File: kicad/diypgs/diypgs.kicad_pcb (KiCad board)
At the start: 2 copper layers, 150 x 78 mm, 15 parts, among them SW1 SW_Push_Dual, SW2 SW_Push_Dual, SW3 SW_Push_Dual, SW4 SW_Push_Dual, SW5 SW_Push_Dual, SW6 SW_Push_Dual, U1 Nokia 5110 LCD

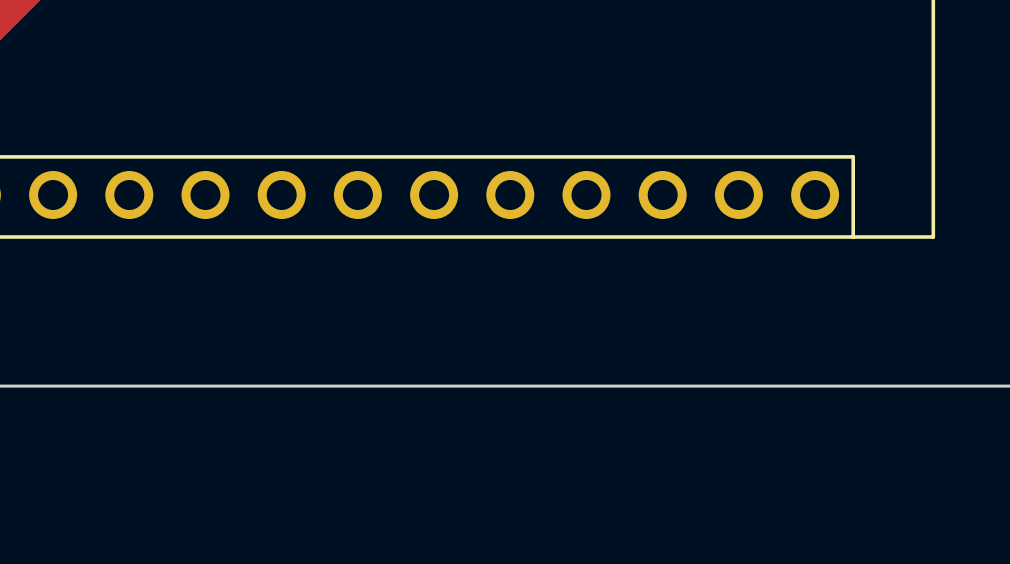
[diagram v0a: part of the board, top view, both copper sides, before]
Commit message: Add JST connector
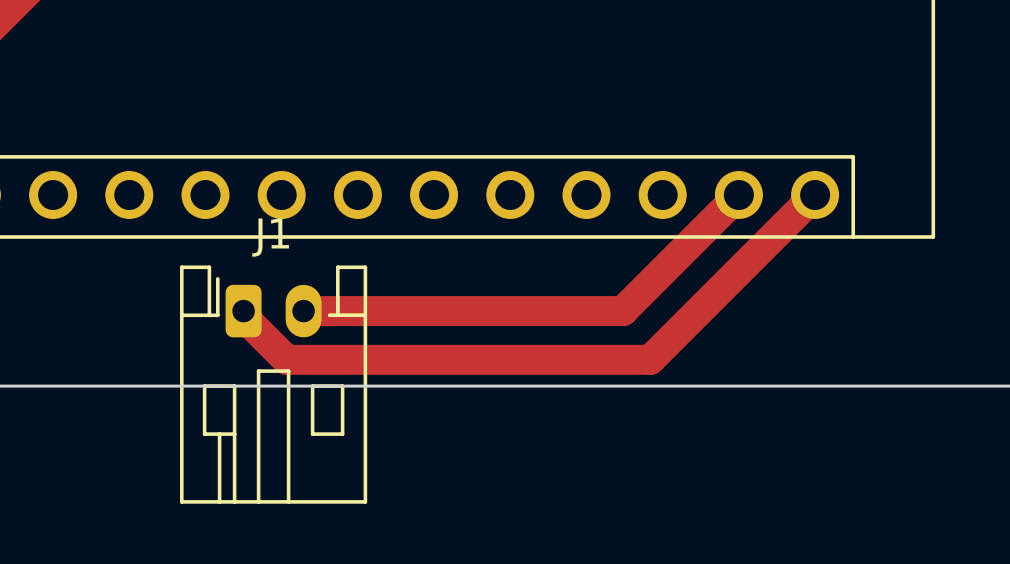
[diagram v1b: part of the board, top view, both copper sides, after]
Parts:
- added J1: Conn_01x02, Connector_JST:JST_PH_S2B-PH-K_1x02_P2.00mm_Horizontal, F.Cu at (124.0, 113.5)
- U1: value Nokia 5110 LCD -> Sparkfun - Graphic LCD 84x48 - Nokia 5110
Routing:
- net VCC: track 0.00 -> 22.1 mm
- net GND: track 303.3 -> 319.4 mm

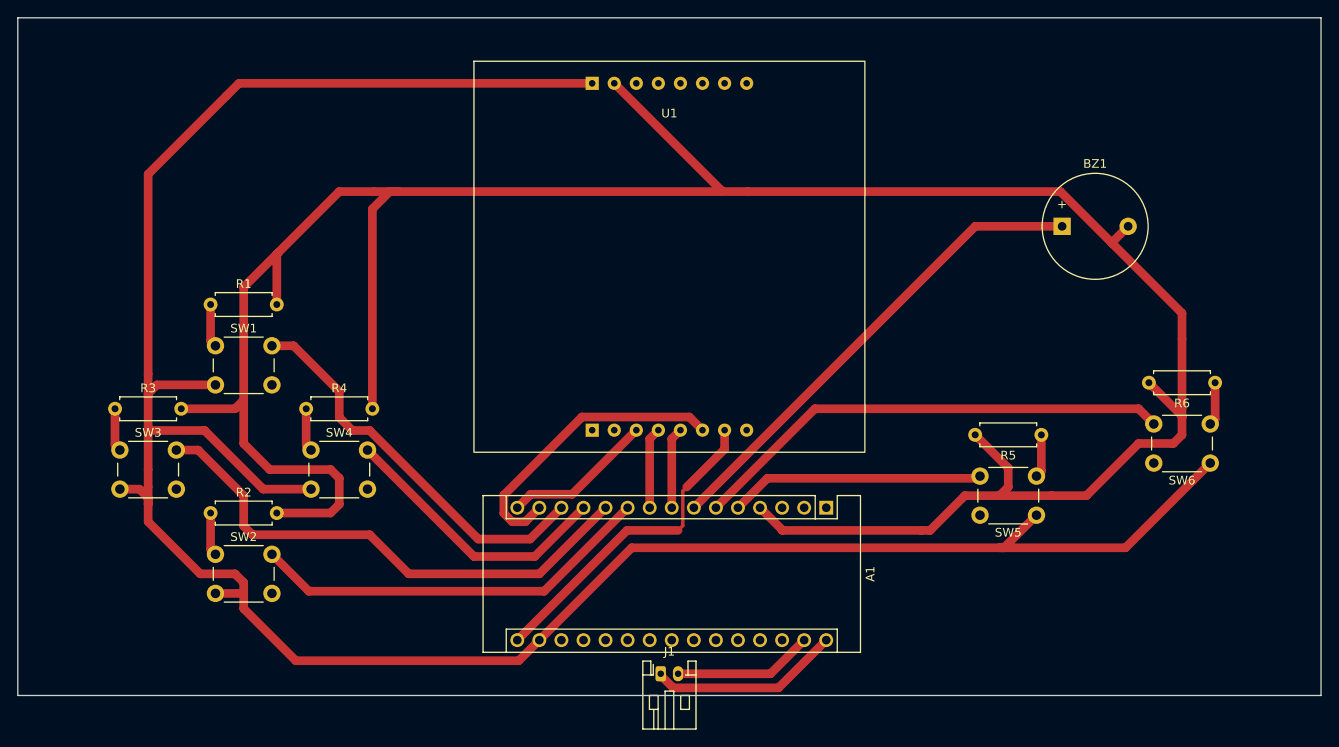
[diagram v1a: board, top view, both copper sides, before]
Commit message: Board modification after initial PCB prototype
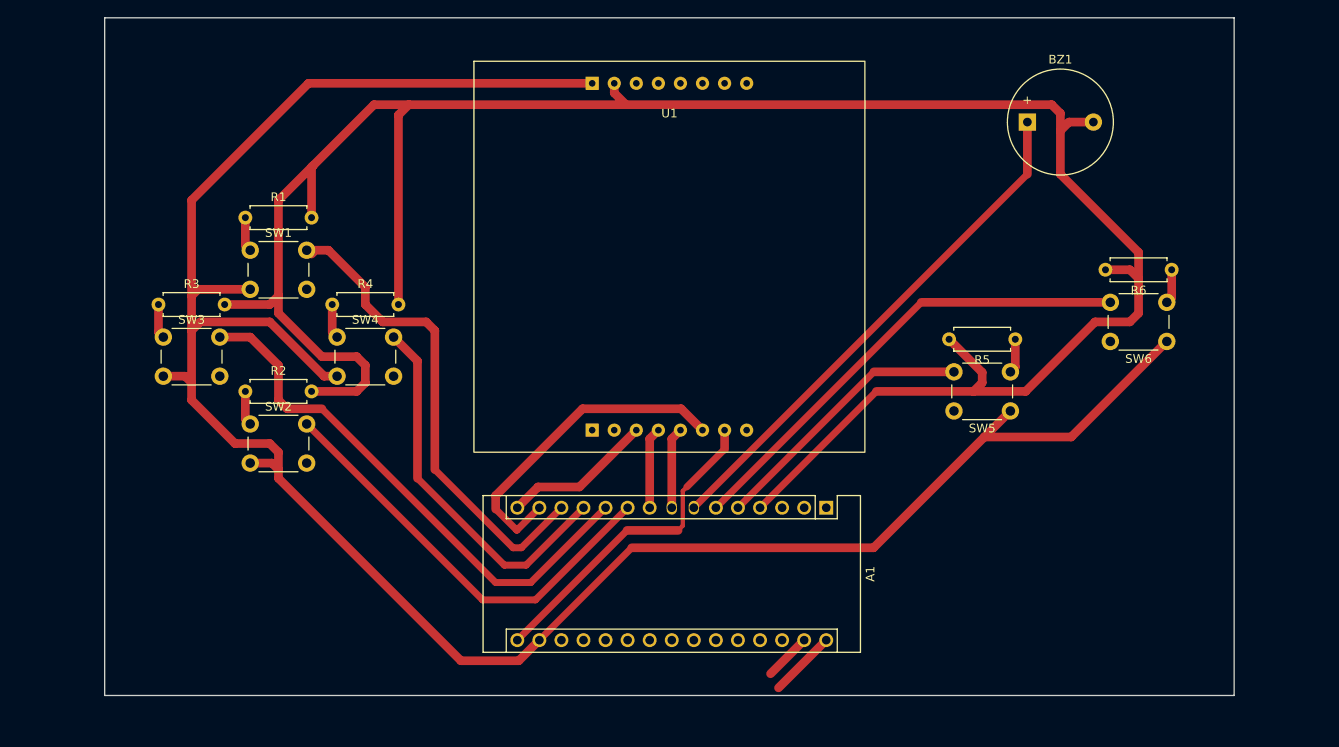
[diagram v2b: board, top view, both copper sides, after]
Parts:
- removed J1: Conn_01x02, Connector_JST:JST_PH_S2B-PH-K_1x02_P2.00mm_Horizontal
- moved SW2 15.5 mm to (76.8, 84.8)
- moved SW6 14.9 mm to (182.2, 75.2)
- moved R2 14.6 mm to (76.2, 81.0)
- moved R6 13.9 mm to (182.8, 67.0)
- moved SW3 13.9 mm to (66.8, 74.8)
- moved SW4 13.3 mm to (86.8, 74.8)
- moved R3 13.0 mm to (66.2, 71.0)
- moved BZ1 12.6 mm to (166.2, 50.0)
- moved R4 12.4 mm to (86.2, 71.0)
- moved SW5 12.4 mm to (164.2, 83.2)
- moved SW1 11.7 mm to (76.8, 64.8)
- moved R5 11.4 mm to (164.8, 75.0)
- moved R1 10.8 mm to (76.2, 61.0)
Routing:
- net GND: track 319.4 -> 269.7 mm
- net +3V3: track 278.5 -> 254.5 mm
- net VCC: track 22.1 -> 7.77 mm
- net /ARDUINO_PAD_RIGHT_PIN: track 32.3 -> 43.4 mm
- net /ARDUINO_PAD_UP_PIN: track 45.8 -> 56.2 mm
- net /ARDUINO_BUZZER_PIN: track 55.8 -> 60.3 mm
- net /ARDUINO_MOSI_PIN: track 34.5 -> 37.6 mm
- net /ARDUINO_PAD_DOWN_PIN: track 46.7 -> 49.7 mm
- net /ARDUINO_PAD_B_PIN: track 29.4 -> 31.6 mm
- net /ARDUINO_PAD_LEFT_PIN: track 60.5 -> 62.0 mm
- net Net-(R6-Pad1): track 4.98 -> 3.98 mm
- net Net-(R5-Pad1): track 4.98 -> 3.98 mm
- net Net-(R4-Pad1): track 4.98 -> 3.98 mm
- net Net-(R3-Pad1): track 4.98 -> 3.98 mm
- net Net-(R2-Pad1): track 4.98 -> 3.98 mm
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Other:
- board size 150 x 78 mm -> 130 x 78 mm

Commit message: Thinner PCB tracks
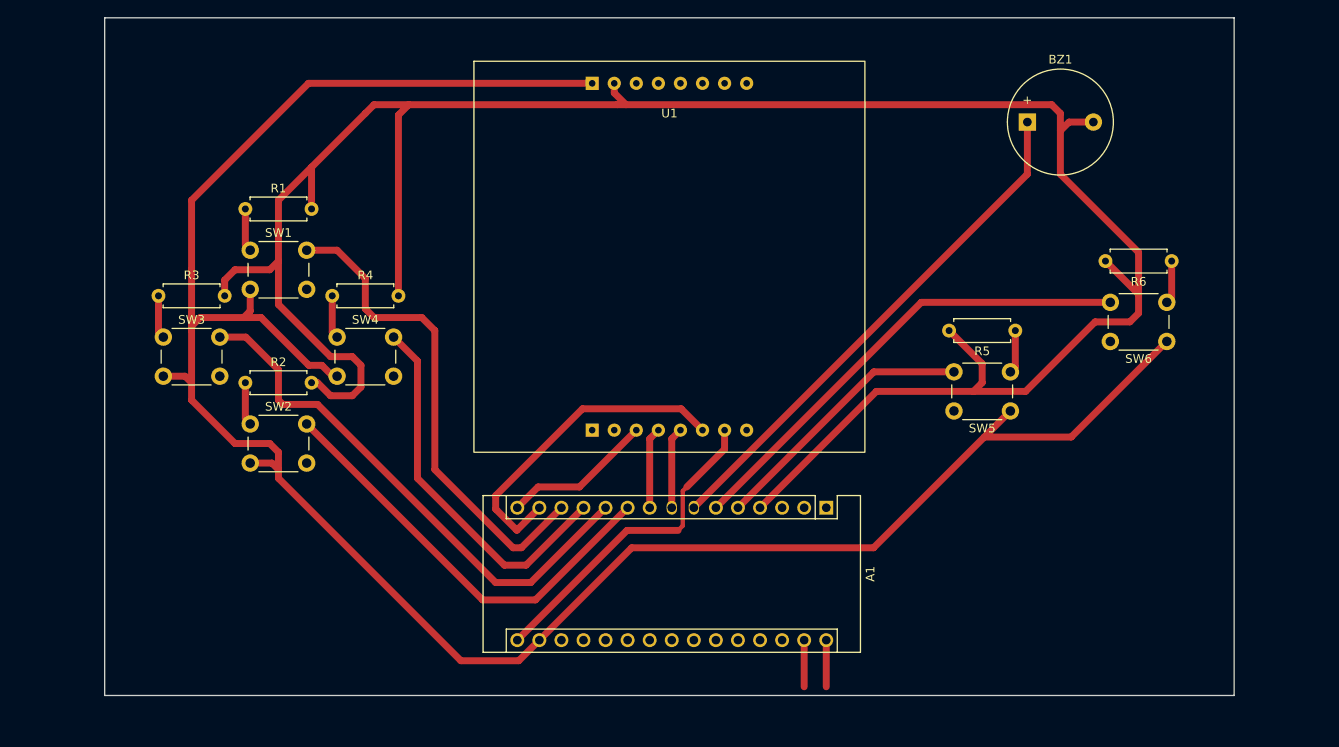
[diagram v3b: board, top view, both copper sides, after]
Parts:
- moved R1 1.00 mm to (76.2, 60.0)
- moved R2 1.00 mm to (76.2, 80.0)
- moved R3 1.00 mm to (66.2, 70.0)
- moved R4 1.00 mm to (86.2, 70.0)
- moved R5 1.00 mm to (164.8, 74.0)
- moved R6 1.00 mm to (182.8, 66.0)
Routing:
- net +3V3: track 254.5 -> 251.4 mm
- net VCC: track 7.77 -> 5.37 mm
- net GND: track 269.7 -> 271.4 mm
- net Net-(R6-Pad1): track 3.98 -> 4.98 mm
- net Net-(R5-Pad1): track 3.98 -> 4.98 mm
- net Net-(R4-Pad1): track 3.98 -> 4.98 mm
- net Net-(R3-Pad1): track 3.98 -> 4.98 mm
- net Net-(R2-Pad1): track 3.98 -> 4.98 mm
- net Net-(R1-Pad1): track 3.98 -> 4.98 mm
- net /ARDUINO_PAD_UP_PIN: track 56.2 -> 56.8 mm

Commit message: Move tracks to background layer
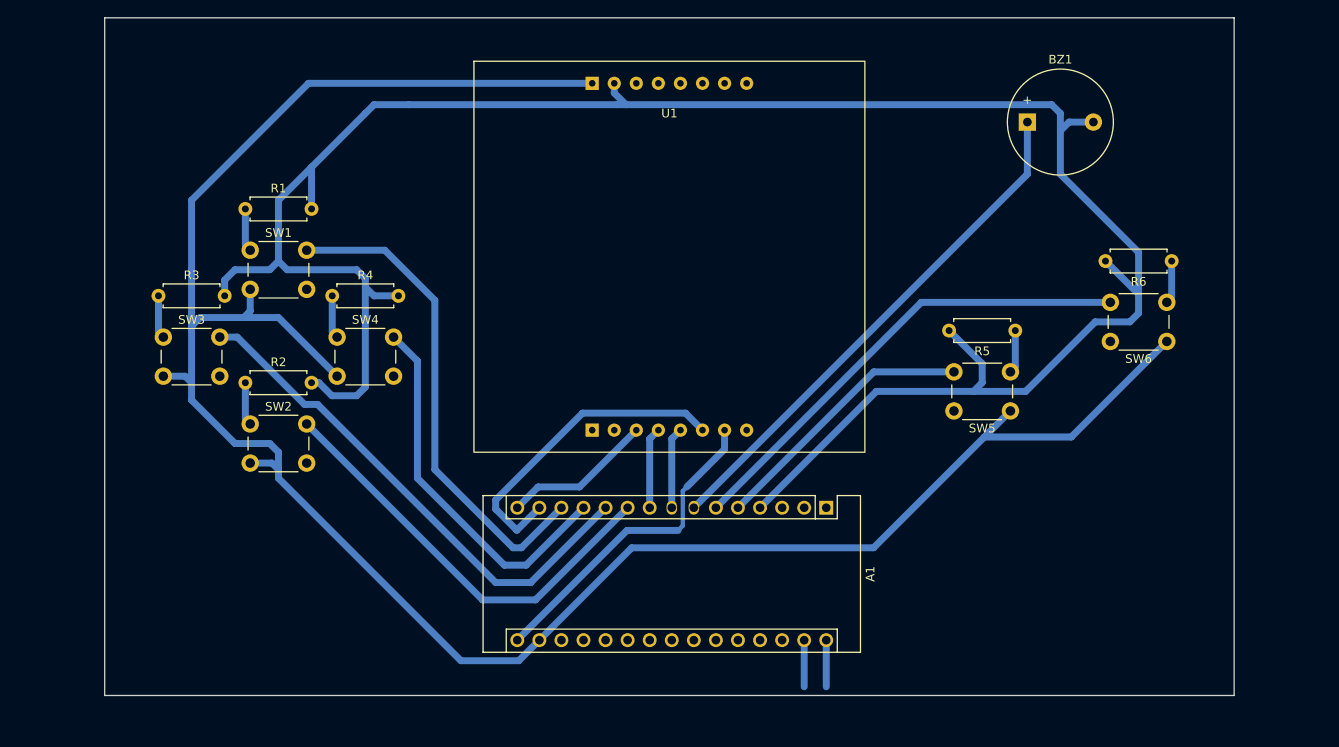
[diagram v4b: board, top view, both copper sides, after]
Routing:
- net GND: track 271.4 -> 257.0 mm
- net /ARDUINO_PAD_LEFT_PIN: track 61.7 -> 59.7 mm
- net /ARDUINO_MOSI_PIN: track 37.6 -> 36.9 mm
